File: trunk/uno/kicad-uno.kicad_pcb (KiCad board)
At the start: 2 copper layers, 68.6 x 53.3 mm, 54 parts, among them J1 RESET_EN, Q1 FDN340P, SW1 RESET, U1 NCP1117 5V, U2 LP2985-33DBVR, U3 ATMEGA16U2-MU(R), U5 LM358, X1 CSTCE16M0V53 16MHz

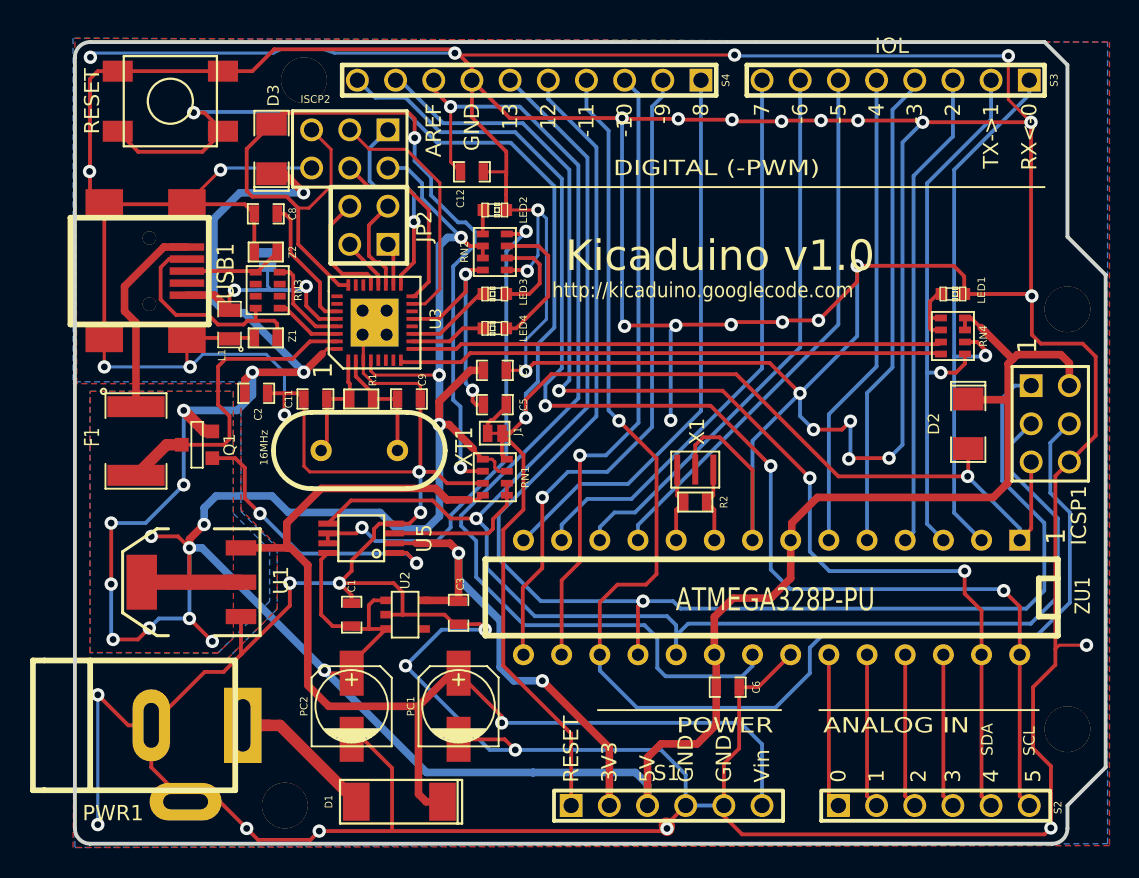
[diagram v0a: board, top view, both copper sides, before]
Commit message: Minor track spacing changes, just to reduce copper etch some.
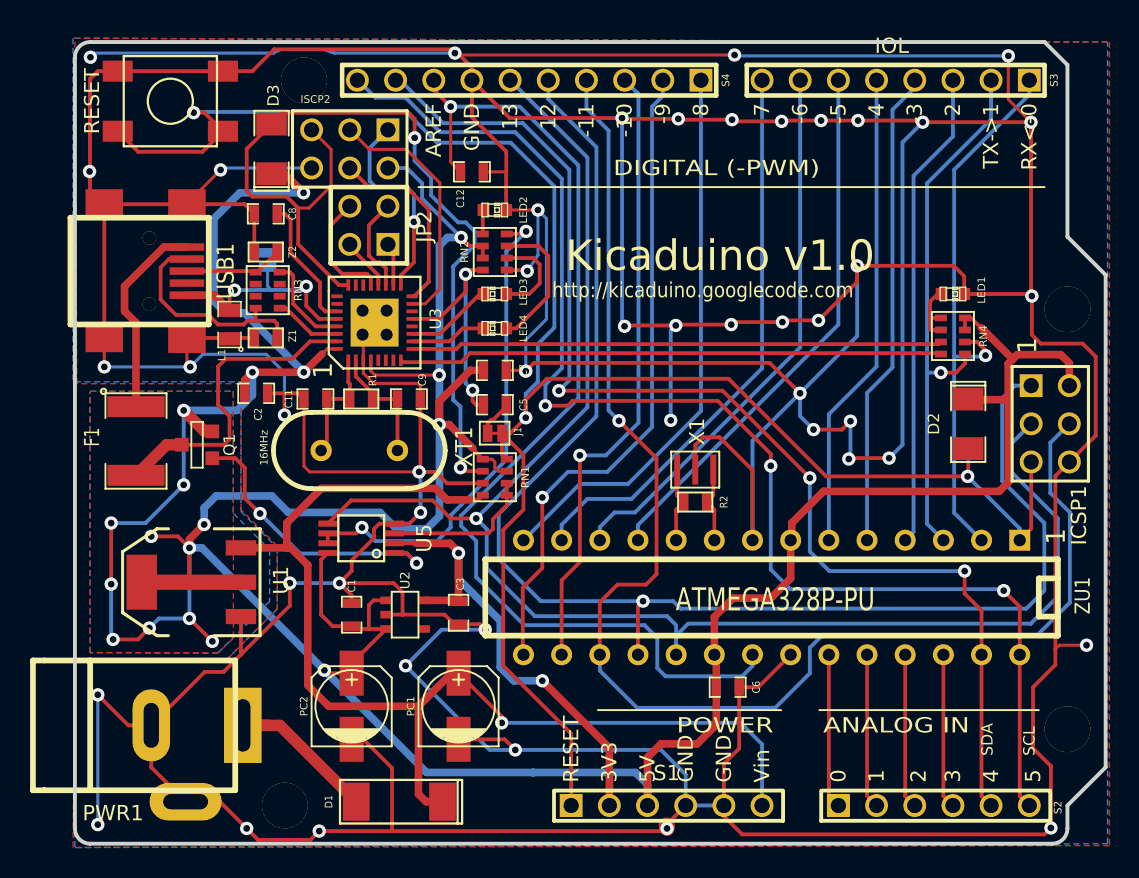
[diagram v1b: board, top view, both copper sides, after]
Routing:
- net /AD5/SCL: track 86.5 -> 87.3 mm
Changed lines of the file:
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@@
     (thickness 1.6)
     (drawings 56)
-    (tracks 966)
+    (tracks 969)
     (zones 0)
     (modules 54)
@@
   (layers
     (15 F.Cu signal)
-    (0 B.Cu signal)
+    (0 B.Cu signal hide)
     (16 B.Adhes user)
     (17 F.Adhes user)
@@
   (segment (start 87.5 49.2) (end 87.5 46.8) (width 0.508) (layer F.Cu) (net 2))
   (segment (start 87.5 54.7) (end 87.5 49.2) (width 0.508) (layer F.Cu) (net 2))
-  (segment (start 86.5 55.7) (end 87.5 54.7) (width 0.508) (layer F.Cu) (net 2))
-  (segment (start 74.8 55.7) (end 86.5 55.7) (width 0.508) (layer F.Cu) (net 2))
-  (segment (start 73.1 57.4) (end 74.8 55.7) (width 0.508) (layer F.Cu) (net 2))
+  (segment (start 86.9064 55.2936) (end 87.5 54.7) (width 0.508) (layer F.Cu) (net 2))
+  (segment (start 75.2064 55.2936) (end 86.9064 55.2936) (width 0.508) (layer F.Cu) (net 2))
+  (segment (start 73.1 57.4) (end 75.2064 55.2936) (width 0.508) (layer F.Cu) (net 2))
   (segment (start 73.1 58.472) (end 73.1 57.4) (width 0.508) (layer F.Cu) (net 2))
   (segment (start 34 57.5) (end 34 56.4) (width 0.508) (layer B.Cu) (net 2))
@@
   (segment (start 86.36 76.2) (end 85.725 75.565) (width 0.254) (layer F.Cu) (net 7))
   (segment (start 85.725 75.565) (end 85.725 66.167) (width 0.254) (layer F.Cu) (net 7))
-  (segment (start 56.7 49.6) (end 67.7 49.6) (width 0.254) (layer F.Cu) (net 8))
+  (segment (start 56.7 49.6) (end 58.1976 49.6) (width 0.254) (layer F.Cu) (net 8))
+  (segment (start 54.7 31.4) (end 57.8 34.5) (width 0.254) (layer B.Cu) (net 8))
+  (segment (start 44.24 27.94) (end 45.4 29.1) (width 0.254) (layer B.Cu) (net 8))
+  (segment (start 45.4 29.1) (end 47.4 29.1) (width 0.254) (layer B.Cu) (net 8))
+  (segment (start 47.4 29.1) (end 49.7 31.4) (width 0.254) (layer B.Cu) (net 8))
+  (segment (start 49.7 31.4) (end 54.7 31.4) (width 0.254) (layer B.Cu) (net 8))
+  (via (at 56.7 49.6) (size 0.889) (layers F.Cu B.Cu) (net 8))
+  (via (at 71.7 53.6) (size 0.889) (layers F.Cu B.Cu) (net 8))
+  (segment (start 71.7 53.6) (end 71.7 60.5) (width 0.254) (layer B.Cu) (net 8))
+  (segment (start 71.7 60.5) (end 73 61.8) (width 0.254) (layer B.Cu) (net 8))
+  (segment (start 73 61.8) (end 87.1 61.8) (width 0.254) (layer B.Cu) (net 8))
+  (segment (start 87.1 61.8) (end 87.2 61.9) (width 0.254) (layer B.Cu) (net 8))
+  (via (at 87.2 61.9) (size 0.889) (layers F.Cu B.Cu) (net 8))
+  (segment (start 87.2 61.9) (end 88.265 62.965) (width 0.254) (layer F.Cu) (net 8))
+  (segment (start 88.265 66.167) (end 88.265 62.965) (width 0.254) (layer F.Cu) (net 8))
+  (segment (start 44.24 27.94) (end 44.196 27.94) (width 0.254) (layer B.Cu) (net 8))
+  (segment (start 56.7 48.2) (end 56.7 49.6) (width 0.254) (layer B.Cu) (net 8))
+  (segment (start 57.8 47.1) (end 56.7 48.2) (width 0.254) (layer B.Cu) (net 8))
   (segment (start 57.8 34.5) (end 57.8 47.1) (width 0.254) (layer B.Cu) (net 8))
-  (segment (start 57.8 47.1) (end 56.7 48.2) (width 0.254) (layer B.Cu) (net 8))
-  (segment (start 56.7 48.2) (end 56.7 49.6) (width 0.254) (layer B.Cu) (net 8))
-  (segment (start 44.196 27.94) (end 44.24 27.94) (width 0.254) (layer B.Cu) (net 8))
-  (segment (start 88.265 62.965) (end 88.265 66.167) (width 0.254) (layer F.Cu) (net 8))
-  (segment (start 87.2 61.9) (end 88.265 62.965) (width 0.254) (layer F.Cu) (net 8))
-  (via (at 87.2 61.9) (size 0.889) (layers F.Cu B.Cu) (net 8))
-  (segment (start 87.1 61.8) (end 87.2 61.9) (width 0.254) (layer B.Cu) (net 8))
-  (segment (start 73 61.8) (end 87.1 61.8) (width 0.254) (layer B.Cu) (net 8))
-  (segment (start 71.7 60.5) (end 73 61.8) (width 0.254) (layer B.Cu) (net 8))
-  (segment (start 71.7 53.6) (end 71.7 60.5) (width 0.254) (layer B.Cu) (net 8))
-  (via (at 71.7 53.6) (size 0.889) (layers F.Cu B.Cu) (net 8))
-  (via (at 56.7 49.6) (size 0.889) (layers F.Cu B.Cu) (net 8))
-  (segment (start 49.7 31.4) (end 54.7 31.4) (width 0.254) (layer B.Cu) (net 8))
-  (segment (start 47.4 29.1) (end 49.7 31.4) (width 0.254) (layer B.Cu) (net 8))
-  (segment (start 45.4 29.1) (end 47.4 29.1) (width 0.254) (layer B.Cu) (net 8))
-  (segment (start 44.24 27.94) (end 45.4 29.1) (width 0.254) (layer B.Cu) (net 8))
-  (segment (start 54.7 31.4) (end 57.8 34.5) (width 0.254) (layer B.Cu) (net 8))
-  (segment (start 67.7 49.6) (end 71.7 53.6) (width 0.254) (layer F.Cu) (net 8))
+  (segment (start 71.7 52.8024) (end 71.7 53.6) (width 0.254) (layer F.Cu) (net 8))
+  (segment (start 68.1736 49.276) (end 71.7 52.8024) (width 0.254) (layer F.Cu) (net 8))
+  (segment (start 58.5216 49.276) (end 68.1736 49.276) (width 0.254) (layer F.Cu) (net 8))
+  (segment (start 58.1976 49.6) (end 58.5216 49.276) (width 0.254) (layer F.Cu) (net 8))
   (segment (start 88.9 76.2) (end 88.265 75.565) (width 0.254) (layer F.Cu) (net 8))
   (segment (start 88.265 75.565) (end 88.265 66.167) (width 0.254) (layer F.Cu) (net 8))
@@
   (segment (start 88.265 58.547) (end 89.027 57.785) (width 0.254) (layer F.Cu) (net 20))
   (segment (start 89.027 57.785) (end 89.027 53.34) (width 0.254) (layer F.Cu) (net 20))
-  (segment (start 84.8 54.3) (end 76.2 54.3) (width 0.254) (layer F.Cu) (net 20))
+  (segment (start 84.8 54.3) (end 75.3872 54.3) (width 0.254) (layer F.Cu) (net 20))
   (segment (start 55.4 49.2) (end 55.4 50.4) (width 0.254) (layer F.Cu) (net 20))
-  (segment (start 57.1 47.5) (end 55.4 49.2) (width 0.254) (layer F.Cu) (net 20))
-  (segment (start 69.4 47.5) (end 57.1 47.5) (width 0.254) (layer F.Cu) (net 20))
-  (segment (start 76.2 54.3) (end 69.4 47.5) (width 0.254) (layer F.Cu) (net 20))
+  (segment (start 56.7952 47.8048) (end 55.4 49.2) (width 0.254) (layer F.Cu) (net 20))
+  (segment (start 68.892 47.8048) (end 56.7952 47.8048) (width 0.254) (layer F.Cu) (net 20))
+  (segment (start 75.3872 54.3) (end 68.892 47.8048) (width 0.254) (layer F.Cu) (net 20))
   (segment (start 88.265 58.547) (end 88.265 57.765) (width 0.254) (layer B.Cu) (net 20))
   (segment (start 84.836 54.264) (end 84.836 52.451) (width 0.254) (layer F.Cu) (net 20))
